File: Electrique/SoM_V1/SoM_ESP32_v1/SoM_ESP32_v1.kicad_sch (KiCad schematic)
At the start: 1 part, among them J101 Bus_M.2_Socket_E

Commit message: changement kicad
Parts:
- added 101: M.2-B-KEY-2280-ADAPTER, symbol m.2_Connector:M.2-B-KEY-2280-ADAPTER
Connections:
- new net: 101.MOUNTING-HOLE (MP1), 101.MOUNTING-HOLE2 (MP1)
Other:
- moved on the sheet: J101
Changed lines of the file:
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@@
 	(text_box "J'ai l'intention de prendre un socket E. Le M.2 bus E standard est celui à droite. Plusieurs de ces ports/connexions seront changées afin de remplir nos besoin. Je garde le connecteur là simplement pour référence.\n\nLa connexion doit avoir:\n- I2C\n- SPI\n- PWM\n- UART\n- USB\n- GPIO\n- RESET\n- Can Bus\n- ..."
 		(exclude_from_sim no)
-		(at 125.73 29.21 0)
+		(at 71.12 20.32 0)
 		(size 45.72 91.44)
 		(stroke
@@
 	)
 	(symbol
+		(lib_id "m.2_Connector:M.2-B-KEY-2280-ADAPTER")
+		(at 187.96 111.76 0)
+		(unit 1)
+		(exclude_from_sim no)
+		(in_bom yes)
+		(on_board yes)
+		(dnp no)
+		(fields_autoplaced yes)
+		(property "Reference" "101"
+			(at 195.58 114.3 0)
+			(effects
+				(font
+					(size 1.778 1.5113)
+				)
+			)
+		)
+		(property "Value" "M.2-B-KEY-2280-ADAPTER"
+			(at 195.58 118.11 0)
+			(effects
+				(font
+					(size 1.778 1.5113)
+				)
+			)
+		)
+		(property "Footprint" ""
+			(at 187.96 111.76 0)
+			(effects
+				(font
+					(size 1.27 1.27)
+				)
+				(hide yes)
+			)
+		)
+		(property "Datasheet" ""
+			(at 187.96 111.76 0)
+			(effects
+				(font
+					(size 1.27 1.27)
+				)
+				(hide yes)
+			)
+		)
+		(property "Description" ""
+			(at 187.96 111.76 0)
+			(effects
+				(font
+					(size 1.27 1.27)
+				)
+				(hide yes)
+			)
+		)
+		(pin "P$28"
+		)
+		(pin "P$31"
+		)
+		(pin "P$33"
+		)
+		(pin "MOUNTING-HOLE2"
+		)
+		(pin "P$56"
+		)
+		(pin "P$43"
+		)
+		(pin "P$59"
+		)
+		(pin "P$42"
+		)
+		(pin "P$22"
+		)
+		(pin "P$44"
+		)
+		(pin "P$37"
+		)
+		(pin "P$40"
+		)
+		(pin "P$34"
+		)
+		(pin "P$41"
+		)
+		(pin "P$61"
+		)
+		(pin "P$4"
+		)
+		(pin "P$66"
+		)
+		(pin "P$69"
+		)
+		(pin "P$52"
+		)
+		(pin "P$70"
+		)
+		(pin "P$49"
+		)
+		(pin "P$20"
+		)
+		(pin "MOUNTING-HOLE"
+		)
+		(pin "P$26"
+		)
+		(pin "P$30"
+		)
+		(pin "P$38"
+		)
+		(pin "P$24"
+		)
+		(pin "P$25"
+		)
+		(pin "P$39"
+		)
+		(pin "P$46"
+		)
+		(pin "P$51"
+		)
+		(pin "P$57"
+		)
+		(pin "P$47"
+		)
+		(pin "P$5"
+		)
+		(pin "P$45"
+		)
+		(pin "P$53"
+		)
+		(pin "P$60"
+		)
+		(pin "P$62"
+		)
+		(pin "P$21"
+		)
+		(pin "P$65"
+		)
+		(pin "P$50"
+		)
+		(pin "P$36"
+		)
+		(pin "P$67"
+		)
+		(pin "P$10"
+		)
+		(pin "P$1"
+		)
+		(pin "P$27"
+		)
+		(pin "P$29"
+		)
+		(pin "P$48"
+		)
+		(pin "P$63"
+		)
+		(pin "P$32"
+		)
+		(pin "P$35"
+		)
+		(pin "P$2"
+		)
+		(pin "P$54"
+		)
+		(pin "P$64"
+		)
+		(pin "P$68"
+		)
+		(pin "P$7"
+		)
+		(pin "P$71"
+		)
+		(pin "P$11"
+		)
+		(pin "P$58"
+		)
+		(pin "P$6"
+		)
+		(pin "P$23"
+		)
+		(pin "P$55"
+		)
+		(pin "P$3"
+		)
+		(pin "P$8"
+		)
+		(pin "P$73"
+		)
+		(pin "P$75"
+		)
+		(pin "P$9"
+		)
+		(pin "P$72"
+		)
+		(pin "P$74"
+		)
+		(instances
+			(project "SoM_ESP32_v1"
+				(path "/ecd44d9a-8113-48e2-a5bb-0de07ce8b9ce"
+					(reference "101")
+					(unit 1)
+				)
+			)
+		)
+	)
+	(symbol
 		(lib_id "Connector:Bus_M.2_Socket_E")
-		(at 97.79 74.93 0)
+		(at 41.91 66.04 0)
 		(unit 1)
 		(exclude_from_sim no)
@@
 		(fields_autoplaced yes)
 		(property "Reference" "J101"
-			(at 99.9841 24.13 0)
+			(at 44.1041 15.24 0)
 			(effects
 				(font
@@
 		)
 		(property "Value" "Bus_M.2_Socket_E"
-			(at 99.9841 26.67 0)
+			(at 44.1041 17.78 0)
 			(effects
 				(font
@@
 		)
 		(property "Footprint" ""
-			(at 97.79 48.26 0)
+			(at 41.91 39.37 0)
 			(effects
 				(font
@@
 		)
 		(property "Datasheet" "http://read.pudn.com/downloads794/doc/project/3133918/PCIe_M.2_Electromechanical_Spec_Rev1.0_Final_11012013_RS_Clean.pdf#page=150"
-			(at 97.79 48.26 0)
+			(at 41.91 39.37 0)
 			(effects
 				(font
@@
 		)
 		(property "Description" "M.2 Socket 1-SD Mechanical Key E"
-			(at 97.79 74.93 0)
-			(effects
-				(font
+			(at 41.91 66.04 0)
+			(effects
+				(font

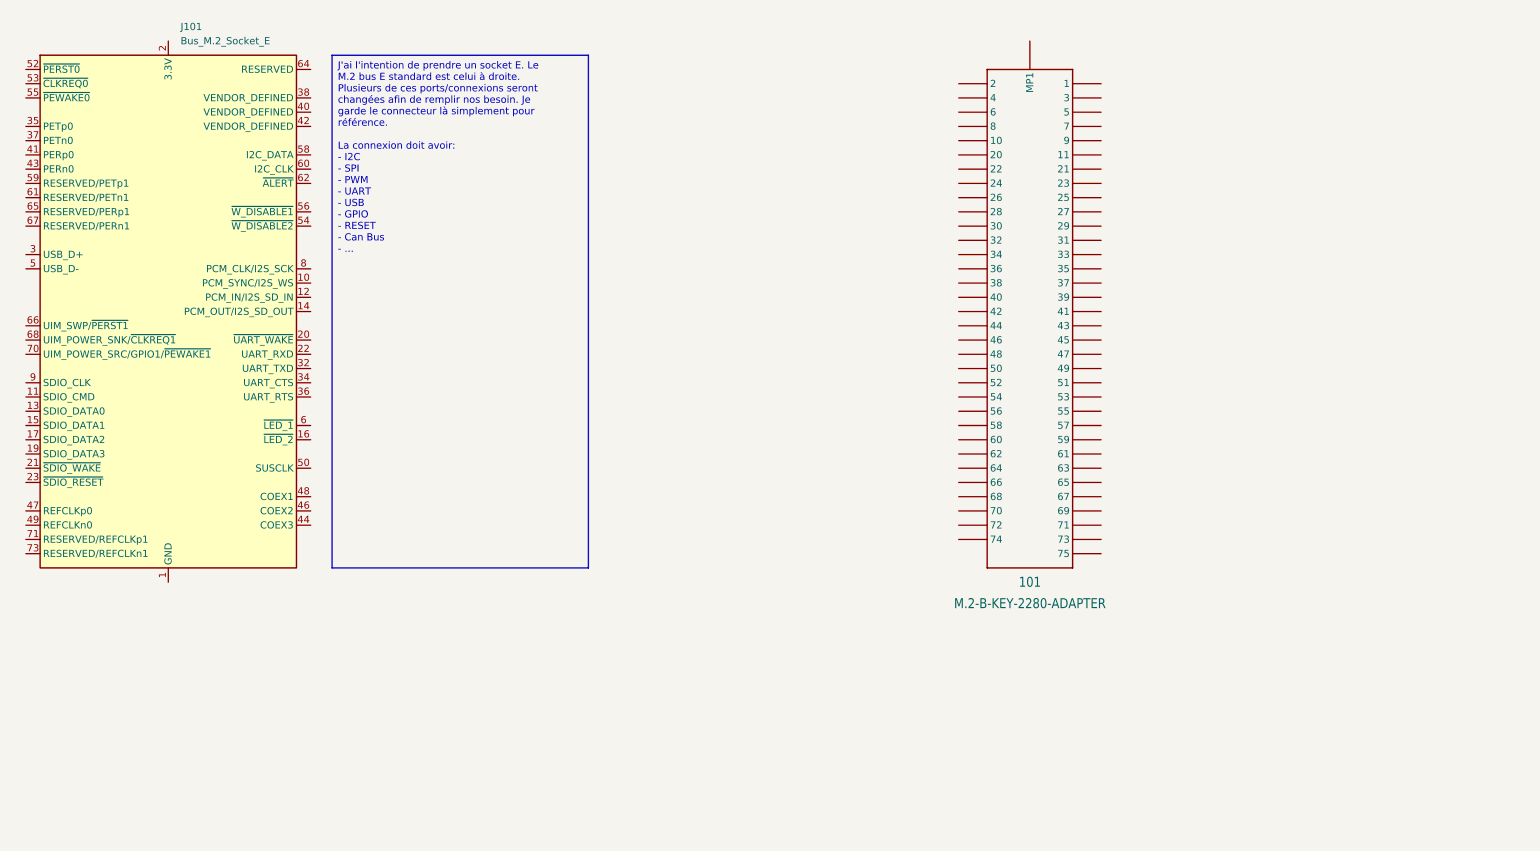
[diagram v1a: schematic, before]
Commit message: push connecteur
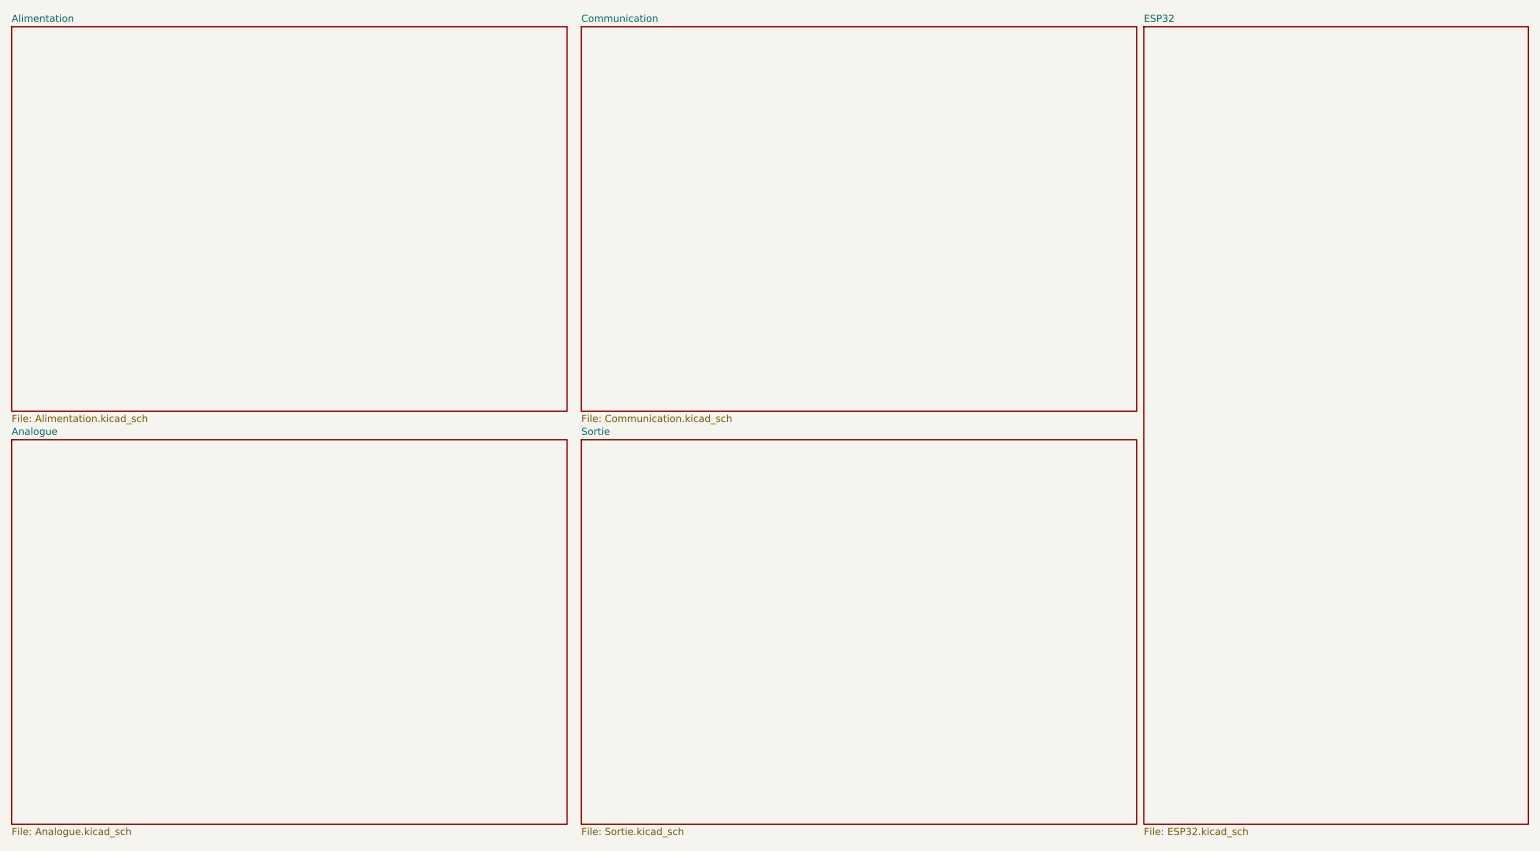
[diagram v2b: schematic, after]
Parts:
- removed 101: M.2-B-KEY-2280-ADAPTER, symbol m.2_Connector:M.2-B-KEY-2280-ADAPTER
- removed J101: Bus_M.2_Socket_E, symbol Connector:Bus_M.2_Socket_E
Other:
- added sheet Alimentation (Alimentation.kicad_sch)
- added sheet Analogue (Analogue.kicad_sch)
- added sheet Communication (Communication.kicad_sch)
- added sheet ESP32 (ESP32.kicad_sch)
- added sheet Sortie (Sortie.kicad_sch)
